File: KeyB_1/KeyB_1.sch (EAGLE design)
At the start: 7 parts

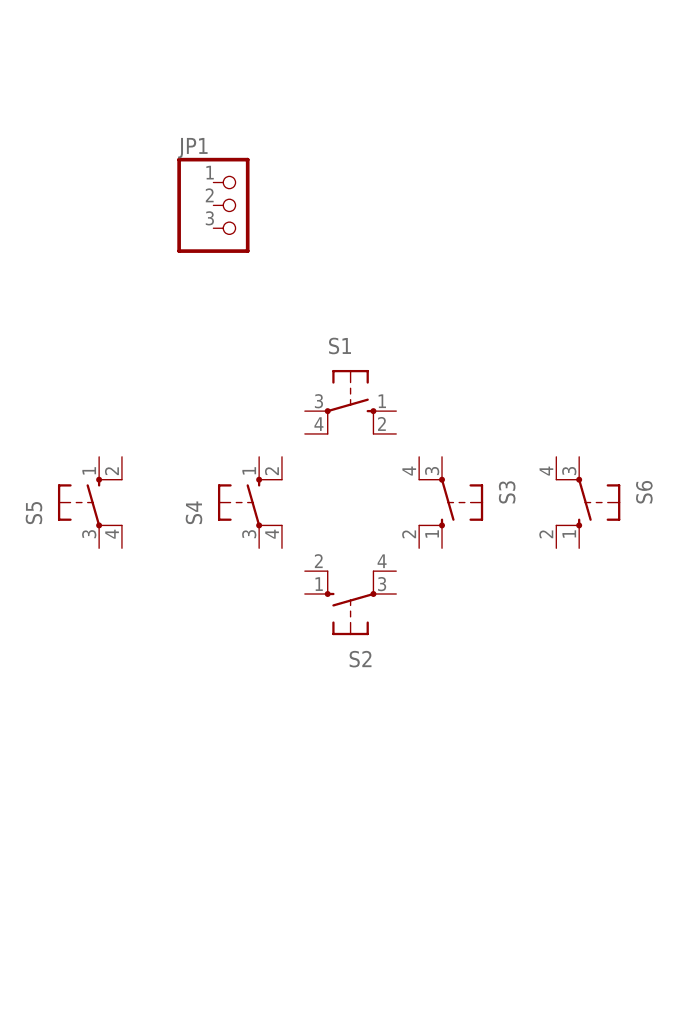
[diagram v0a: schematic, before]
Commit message: changed keyboard schematic
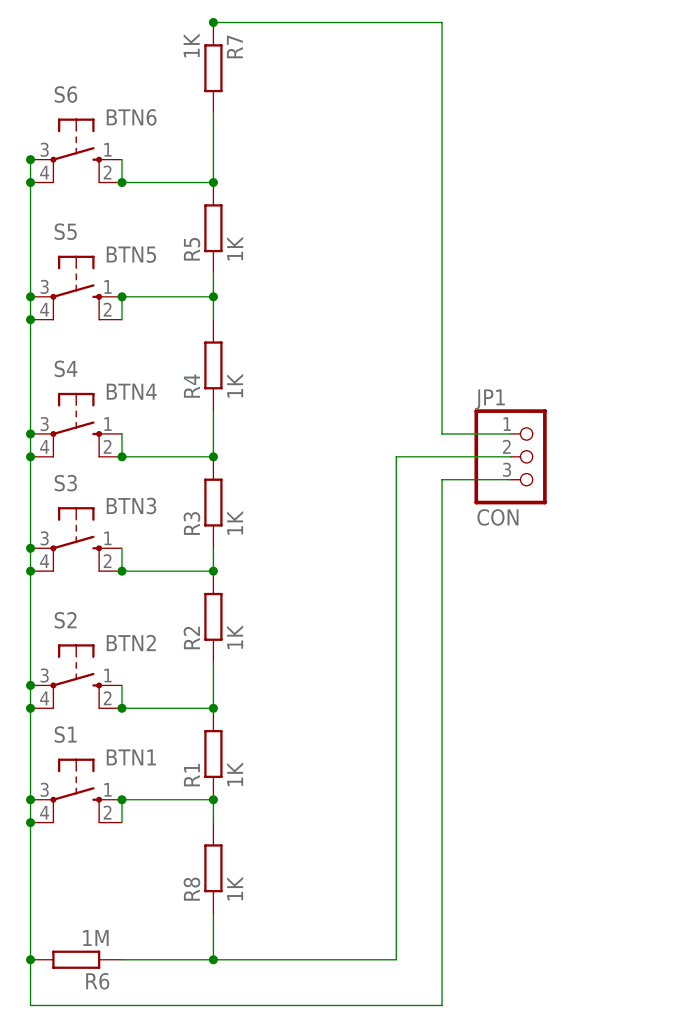
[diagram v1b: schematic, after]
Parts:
- added R1, R2, R3, R4, R5, R7, R8: 1K, rcl:R-EU_R1206W
- added R6: 1M, rcl:R-EU_R1206W
- JP1: value (none) -> CON
- S1: value (none) -> BTN1
- S2: value (none) -> BTN2
- S3: value (none) -> BTN3
- S4: value (none) -> BTN4
- S5: value (none) -> BTN5
- S6: value (none) -> BTN6
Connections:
- new net +5V: JP1.1, R7.1
- new net AN_IN: JP1.3, R6.2, S1.P, S1.P1, S2.P, S2.P1, S3.P, S3.P1, S4.P, S4.P1, S5.P, S5.P1, S6.P, S6.P1
- new net GND: JP1.2, R6.1, R8.1
- new net N$1: R5.2, R7.2, S6.S, S6.S1
- new net N$2: R4.2, R5.1, S5.S, S5.S1
- new net N$3: R2.2, R3.1, S3.S, S3.S1
- new net N$4: R3.2, R4.1, S4.S, S4.S1
- new net N$5: R1.1, R8.2, S1.S, S1.S1
- new net N$7: R1.2, R2.1, S2.S, S2.S1
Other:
- moved on the sheet: JP1, S1, S2, S3, S4, S5, S6
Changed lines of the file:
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@@
 </classes>
 <parts>
-<part name="S1" library="switch-omron" deviceset="10-XX" device=""/>
-<part name="S2" library="switch-omron" deviceset="10-XX" device=""/>
-<part name="S3" library="switch-omron" deviceset="10-XX" device=""/>
-<part name="S4" library="switch-omron" deviceset="10-XX" device=""/>
-<part name="S5" library="switch-omron" deviceset="10-XX" device=""/>
-<part name="S6" library="switch-omron" deviceset="10-XX" device=""/>
-<part name="JP1" library="pinhead" deviceset="PINHD-1X3" device=""/>
+<part name="S1" library="switch-omron" deviceset="10-XX" device="" value="BTN1"/>
+<part name="S2" library="switch-omron" deviceset="10-XX" device="" value="BTN2"/>
+<part name="S3" library="switch-omron" deviceset="10-XX" device="" value="BTN3"/>
+<part name="S4" library="switch-omron" deviceset="10-XX" device="" value="BTN4"/>
+<part name="S5" library="switch-omron" deviceset="10-XX" device="" value="BTN5"/>
+<part name="S6" library="switch-omron" deviceset="10-XX" device="" value="BTN6"/>
+<part name="JP1" library="pinhead" deviceset="PINHD-1X3" device="" value="CON"/>
+<part name="R1" library="rcl" deviceset="R-EU_" device="R1206W" value="1K"/>
+<part name="R2" library="rcl" deviceset="R-EU_" device="R1206W" value="1K"/>
+<part name="R3" library="rcl" deviceset="R-EU_" device="R1206W" value="1K"/>
+<part name="R4" library="rcl" deviceset="R-EU_" device="R1206W" value="1K"/>
+<part name="R5" library="rcl" deviceset="R-EU_" device="R1206W" value="1K"/>
+<part name="R6" library="rcl" deviceset="R-EU_" device="R1206W" value="1M"/>
+<part name="R7" library="rcl" deviceset="R-EU_" device="R1206W" value="1K"/>
+<part name="R8" library="rcl" deviceset="R-EU_" device="R1206W" value="1K"/>
 </parts>
 <sheets>
@@
 </plain>
 <instances>
-<instance part="S1" gate="1" x="53.34" y="40.64" rot="R270"/>
-<instance part="S2" gate="1" x="53.34" y="20.32" rot="R90"/>
-<instance part="S3" gate="1" x="63.5" y="30.48" rot="R180"/>
-<instance part="S4" gate="1" x="43.18" y="30.48"/>
-<instance part="S5" gate="1" x="25.4" y="30.48"/>
-<instance part="S6" gate="1" x="78.74" y="30.48" rot="R180"/>
-<instance part="JP1" gate="A" x="40.64" y="63.5"/>
+<instance part="S1" gate="1" x="22.86" y="-2.54" rot="R270"/>
+<instance part="S2" gate="1" x="22.86" y="10.16" rot="R270"/>
+<instance part="S3" gate="1" x="22.86" y="25.4" rot="R270"/>
+<instance part="S4" gate="1" x="22.86" y="38.1" rot="R270"/>
+<instance part="S5" gate="1" x="22.86" y="53.34" rot="R270"/>
+<instance part="S6" gate="1" x="22.86" y="68.58" rot="R270"/>
+<instance part="JP1" gate="A" x="73.66" y="35.56"/>
+<instance part="R1" gate="G$1" x="38.1" y="2.54" rot="R90"/>
+<instance part="R2" gate="G$1" x="38.1" y="17.78" rot="R90"/>
+<instance part="R3" gate="G$1" x="38.1" y="30.48" rot="R90"/>
+<instance part="R4" gate="G$1" x="38.1" y="45.72" rot="R90"/>
+<instance part="R5" gate="G$1" x="38.1" y="60.96" rot="R90"/>
+<instance part="R6" gate="G$1" x="22.86" y="-20.32" rot="R180"/>
+<instance part="R7" gate="G$1" x="38.1" y="78.74" rot="R270"/>
+<instance part="R8" gate="G$1" x="38.1" y="-10.16" rot="R90"/>
 </instances>
 <busses>
 </busses>
 <nets>
+<net name="+5V" class="0">
+<segment>
+<pinref part="R7" gate="G$1" pin="1"/>
+<wire x1="38.1" y1="83.82" x2="63.5" y2="83.82" width="0.1524" layer="91"/>
+<wire x1="63.5" y1="83.82" x2="63.5" y2="38.1" width="0.1524" layer="91"/>
+<pinref part="JP1" gate="A" pin="1"/>
+<wire x1="63.5" y1="38.1" x2="71.12" y2="38.1" width="0.1524" layer="91"/>
+<junction x="38.1" y="83.82"/>
+</segment>
+</net>
+<net name="N$1" class="0">
+<segment>
+<pinref part="S6" gate="1" pin="S"/>
+<pinref part="S6" gate="1" pin="S1"/>
+<wire x1="27.94" y1="68.58" x2="27.94" y2="66.04" width="0.1524" layer="91"/>
+<pinref part="R5" gate="G$1" pin="2"/>
+<wire x1="27.94" y1="66.04" x2="38.1" y2="66.04" width="0.1524" layer="91"/>
+<pinref part="R7" gate="G$1" pin="2"/>
+<wire x1="38.1" y1="66.04" x2="38.1" y2="73.66" width="0.1524" layer="91"/>
+<junction x="38.1" y="66.04"/>
+<junction x="27.94" y="66.04"/>
+</segment>
+</net>
+<net name="N$2" class="0">
+<segment>
+<pinref part="S5" gate="1" pin="S"/>
+<pinref part="S5" gate="1" pin="S1"/>
+<wire x1="27.94" y1="53.34" x2="27.94" y2="50.8" width="0.1524" layer="91"/>
+<pinref part="R5" gate="G$1" pin="1"/>
+<wire x1="27.94" y1="53.34" x2="38.1" y2="53.34" width="0.1524" layer="91"/>
+<wire x1="38.1" y1="53.34" x2="38.1" y2="55.88" width="0.1524" layer="91"/>
+<pinref part="R4" gate="G$1" pin="2"/>
+<wire x1="38.1" y1="53.34" x2="38.1" y2="50.8" width="0.1524" layer="91"/>
+<junction x="38.1" y="53.34"/>
+<junction x="27.94" y="53.34"/>
+</segment>
+</net>
+<net name="N$3" class="0">
+<segment>
+<pinref part="R3" gate="G$1" pin="1"/>
+<pinref part="R2" gate="G$1" pin="2"/>
+<wire x1="38.1" y1="25.4" x2="38.1" y2="22.86" width="0.1524" layer="91"/>
+<pinref part="S3" gate="1" pin="S"/>
+<pinref part="S3" gate="1" pin="S1"/>
+<wire x1="27.94" y1="25.4" x2="27.94" y2="22.86" width="0.1524" layer="91"/>
+<wire x1="27.94" y1="22.86" x2="38.1" y2="22.86" width="0.1524" layer="91"/>
+<junction x="38.1" y="22.86"/>
+<junction x="27.94" y="22.86"/>
+</segment>
+</net>
+<net name="N$4" class="0">
+<segment>
+<pinref part="R3" gate="G$1" pin="2"/>
+<pinref part="R4" gate="G$1" pin="1"/>
+<wire x1="38.1" y1="35.56" x2="38.1" y2="40.64" width="0.1524" layer="91"/>
+<pinref part="S4" gate="1" pin="S"/>
+<pinref part="S4" gate="1" pin="S1"/>
+<wire x1="27.94" y1="38.1" x2="27.94" y2="35.56" width="0.1524" layer="91"/>
+<wire x1="27.94" y1="35.56" x2="38.1" y2="35.56" width="0.1524" layer="91"/>
+<junction x="38.1" y="35.56"/>
+<junction x="27.94" y="35.56"/>
+</segment>
+</net>
+<net name="N$7" class="0">
+<segment>
+<pinref part="S2" gate="1" pin="S"/>
+<pinref part="S2" gate="1" pin="S1"/>
+<wire x1="27.94" y1="10.16" x2="27.94" y2="7.62" width="0.1524" layer="91"/>
+<pinref part="R1" gate="G$1" pin="2"/>
+<wire x1="27.94" y1="7.62" x2="38.1" y2="7.62" width="0.1524" layer="91"/>
+<pinref part="R2" gate="G$1" pin="1"/>
+<wire x1="38.1" y1="7.62" x2="38.1" y2="12.7" width="0.1524" layer="91"/>
+<junction x="38.1" y="7.62"/>
+<junction x="27.94" y="7.62"/>
+</segment>
+</net>
+<net name="N$5" class="0">
+<segment>
+<pinref part="R1" gate="G$1" pin="1"/>
+<pinref part="S1" gate="1" pin="S"/>
+<wire x1="27.94" y1="-2.54" x2="38.1" y2="-2.54" width="0.1524" layer="91"/>
+<pinref part="S1" gate="1" pin="S1"/>
+<wire x1="27.94" y1="-5.08" x2="27.94" y2="-2.54" width="0.1524" layer="91"/>
+<pinref part="R8" gate="G$1" pin="2"/>
+<wire x1="38.1" y1="-2.54" x2="38.1" y2="-5.08" width="0.1524" layer="91"/>
+<junction x="38.1" y="-2.54"/>
+<junction x="27.94" y="-2.54"/>
+</segment>
+</net>
+<net name="GND" class="0">
+<segment>
+<pinref part="R6" gate="G$1" pin="1"/>
+<pinref part="R8" gate="G$1" pin="1"/>
+<wire x1="27.94" y1="-20.32" x2="38.1" y2="-20.32" width="0.1524" layer="91"/>
+<wire x1="38.1" y1="-20.32" x2="38.1" y2="-15.24" width="0.1524" layer="91"/>
+<wire x1="38.1" y1="-20.32" x2="58.42" y2="-20.32" width="0.1524" layer="91"/>
+<wire x1="58.42" y1="-20.32" x2="58.42" y2="35.56" width="0.1524" layer="91"/>
+<pinref part="JP1" gate="A" pin="2"/>
+<wire x1="58.42" y1="35.56" x2="71.12" y2="35.56" width="0.1524" layer="91"/>
+<junction x="38.1" y="-20.32"/>
+</segment>
+</net>
+<net name="AN_IN" class="0">
+<segment>
+<pinref part="S1" gate="1" pin="P1"/>
+<pinref part="S1" gate="1" pin="P"/>
+<wire x1="17.78" y1="-5.08" x2="17.78" y2="-2.54" width="0.1524" layer="91"/>
+<pinref part="S2" gate="1" pin="P1"/>
+<wire x1="17.78" y1="-2.54" x2="17.78" y2="7.62" width="0.1524" layer="91"/>
+<pinref part="S2" gate="1" pin="P"/>
+<wire x1="17.78" y1="7.62" x2="17.78" y2="10.16" width="0.1524" layer="91"/>
+<pinref part="S3" gate="1" pin="P1"/>
+<wire x1="17.78" y1="10.16" x2="17.78" y2="22.86" width="0.1524" layer="91"/>
+<pinref part="S3" gate="1" pin="P"/>
+<wire x1="17.78" y1="22.86" x2="17.78" y2="25.4" width="0.1524" layer="91"/>
+<pinref part="S4" gate="1" pin="P1"/>
+<wire x1="17.78" y1="25.4" x2="17.78" y2="35.56" width="0.1524" layer="91"/>
+<pinref part="S4" gate="1" pin="P"/>
+<wire x1="17.78" y1="35.56" x2="17.78" y2="38.1" width="0.1524" layer="91"/>
+<pinref part="S5" gate="1" pin="P1"/>
+<wire x1="17.78" y1="38.1" x2="17.78" y2="50.8" width="0.1524" layer="91"/>
+<pinref part="S5" gate="1" pin="P"/>
+<wire x1="17.78" y1="50.8" x2="17.78" y2="53.34" width="0.1524" layer="91"/>
+<pinref part="S6" gate="1" pin="P1"/>
+<wire x1="17.78" y1="53.34" x2="17.78" y2="66.04" width="0.1524" layer="91"/>
+<pinref part="S6" gate="1" pin="P"/>
+<wire x1="17.78" y1="66.04" x2="17.78" y2="68.58" width="0.1524" layer="91"/>
+<wire x1="17.78" y1="-5.08" x2="17.78" y2="-20.32" width="0.1524" layer="91"/>
+<pinref part="R6" gate="G$1" pin="2"/>
+<wire x1="17.78" y1="-20.32" x2="17.78" y2="-25.4" width="0.1524" layer="91"/>
+<junction x="17.78" y="-20.32"/>
+<wire x1="17.78" y1="-25.4" x2="63.5" y2="-25.4" width="0.1524" layer="91"/>
+<wire x1="63.5" y1="-25.4" x2="63.5" y2="33.02" width="0.1524" layer="91"/>
+<pinref part="JP1" gate="A" pin="3"/>
+<wire x1="63.5" y1="33.02" x2="71.12" y2="33.02" width="0.1524" layer="91"/>
+<junction x="17.78" y="68.58"/>
+<junction x="17.78" y="66.04"/>
+<junction x="17.78" y="53.34"/>
+<junction x="17.78" y="50.8"/>
+<junction x="17.78" y="38.1"/>
+<junction x="17.78" y="35.56"/>
+<junction x="17.78" y="25.4"/>
+<junction x="17.78" y="22.86"/>
+<junction x="17.78" y="10.16"/>
+<junction x="17.78" y="7.62"/>
+<junction x="17.78" y="-2.54"/>
+<junction x="17.78" y="-5.08"/>
+</segment>
+</net>
 </nets>
 </sheet>

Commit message: finished layout
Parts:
- S1: value BTN1 -> UP
- S2: value BTN2 -> CANCEL
- S3: value BTN3 -> RIGHT
- S4: value BTN4 -> DOWN
- S5: value BTN5 -> LEFT
- S6: value BTN6 -> OK
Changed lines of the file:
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@@
 </classes>
 <parts>
-<part name="S1" library="switch-omron" deviceset="10-XX" device="" value="BTN1"/>
-<part name="S2" library="switch-omron" deviceset="10-XX" device="" value="BTN2"/>
-<part name="S3" library="switch-omron" deviceset="10-XX" device="" value="BTN3"/>
-<part name="S4" library="switch-omron" deviceset="10-XX" device="" value="BTN4"/>
-<part name="S5" library="switch-omron" deviceset="10-XX" device="" value="BTN5"/>
-<part name="S6" library="switch-omron" deviceset="10-XX" device="" value="BTN6"/>
+<part name="S1" library="switch-omron" deviceset="10-XX" device="" value="UP"/>
+<part name="S2" library="switch-omron" deviceset="10-XX" device="" value="CANCEL"/>
+<part name="S3" library="switch-omron" deviceset="10-XX" device="" value="RIGHT"/>
+<part name="S4" library="switch-omron" deviceset="10-XX" device="" value="DOWN"/>
+<part name="S5" library="switch-omron" deviceset="10-XX" device="" value="LEFT"/>
+<part name="S6" library="switch-omron" deviceset="10-XX" device="" value="OK"/>
 <part name="JP1" library="pinhead" deviceset="PINHD-1X3" device="" value="CON"/>
 <part name="R1" library="rcl" deviceset="R-EU_" device="R1206W" value="1K"/>
